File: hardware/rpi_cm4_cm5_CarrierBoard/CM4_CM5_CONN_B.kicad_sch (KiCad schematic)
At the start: 26 parts, among them J12 RPI_CMx_B

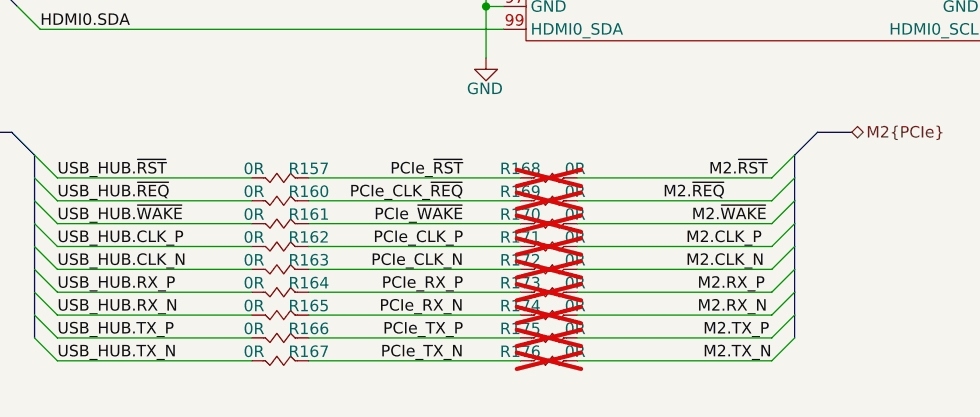
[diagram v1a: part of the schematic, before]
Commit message: Add preliminary output files (PCB PDF, Gerbers, IPC-D-356, IPC-2581, Pick_N_Place, etc) Update BOM, SCH PDF Commit PCB design and set to "Review" state
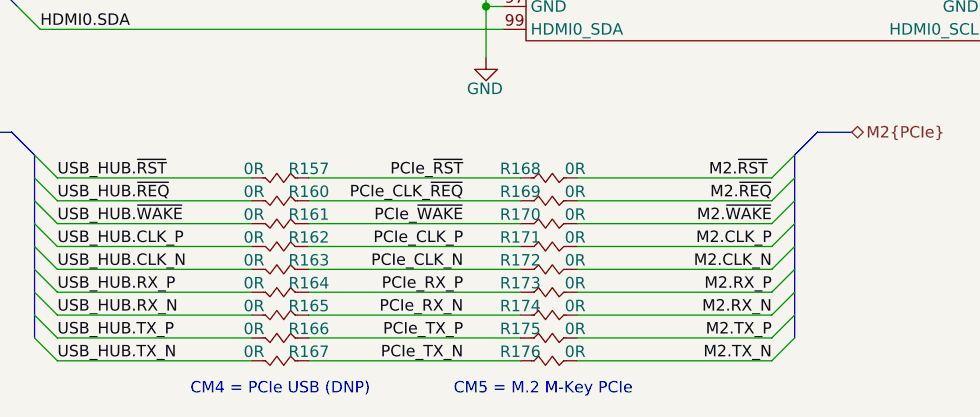
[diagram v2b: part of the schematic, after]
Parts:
- R168, R169, R170, R171, R172, R173, R174, R175, R176: now fitted
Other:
- note added: "CM4 = PCIe USB (DNP)"
- note added: "CM5 = M.2 M-Key PCIe"
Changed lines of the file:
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@@
 	(title_block
 		(title "RPI CMx Carrier")
-		(date "2026-02-13")
+		(date "2026-02-15")
 		(rev "2.00-0A")
 		(comment 1 "Jean-Francois Bilodeau")
@@
 		(comment 6 "Jean-Francois Bilodeau")
 		(comment 7 "Not applicable")
-		(comment 8 "Preliminary")
+		(comment 8 "Released")
 		(comment 9 "RPI_CMx_Carrier_2.00-0A_BOM")
 	)
@@
 		)
 	)
+	(text "CM4 = PCIe USB (DNP)"
+		(exclude_from_sim no)
+		(at 100.33 189.23 0)
+		(effects
+			(font
+				(size 1.27 1.27)
+				(color 255 153 0 1)
+			)
+		)
+	)
+	(text "CM5 = M.2 M-Key PCIe"
+		(exclude_from_sim no)
+		(at 129.54 189.23 0)
+		(effects
+			(font
+				(size 1.27 1.27)
+				(color 255 153 0 1)
+			)
+		)
+	)
 	(junction
 		(at 182.88 55.245)
@@
 	)
 	(label "M2.~{WAKE}"
-		(at 146.05 170.815 0)
+		(at 154.94 170.815 180)
 		(effects
 			(font
 				(size 1.27 1.27)
 			)
-			(justify left bottom)
+			(justify right bottom)
 		)
 	)
@@
 	)
 	(label "M2.CLK_N"
-		(at 145.415 175.895 0)
+		(at 154.94 175.895 180)
 		(effects
 			(font
 				(size 1.27 1.27)
 			)
-			(justify left bottom)
+			(justify right bottom)
 		)
 	)
@@
 	)
 	(label "M2.CLK_P"
-		(at 145.415 173.355 0)
+		(at 154.94 173.355 180)
 		(effects
 			(font
 				(size 1.27 1.27)
 			)
-			(justify left bottom)
+			(justify right bottom)
 		)
 	)
@@
 	)
 	(label "M2.TX_N"
-		(at 147.32 186.055 0)
+		(at 154.94 186.055 180)
 		(effects
 			(font
 				(size 1.27 1.27)
 			)
-			(justify left bottom)
+			(justify right bottom)
 		)
 	)
@@
 	)
 	(label "M2.~{REQ}"
-		(at 142.875 168.275 0)
+		(at 154.94 168.275 180)
 		(effects
 			(font
 				(size 1.27 1.27)
 			)
-			(justify left bottom)
+			(justify right bottom)
 		)
 	)
@@
 	)
 	(label "M2.TX_P"
-		(at 147.32 183.515 0)
+		(at 154.94 183.515 180)
 		(effects
 			(font
 				(size 1.27 1.27)
 			)
-			(justify left bottom)
+			(justify right bottom)
 		)
 	)
 	(label "M2.RX_P"
-		(at 146.685 178.435 0)
+		(at 154.94 178.435 180)
 		(effects
 			(font
 				(size 1.27 1.27)
 			)
-			(justify left bottom)
+			(justify right bottom)
 		)
 	)
 	(label "M2.RX_N"
-		(at 146.685 180.975 0)
+		(at 154.94 180.975 180)
 		(effects
 			(font
 				(size 1.27 1.27)
 			)
-			(justify left bottom)
+			(justify right bottom)
 		)
 	)
@@
 		(in_bom yes)
 		(on_board yes)
-		(dnp yes)
+		(dnp no)
 		(property "Reference" "R176"
 			(at 127 185.039 0)
@@
 		(in_bom yes)
 		(on_board yes)
-		(dnp yes)
+		(dnp no)
 		(property "Reference" "R173"
 			(at 127 177.419 0)
@@
 		(in_bom yes)
 		(on_board yes)
-		(dnp yes)
+		(dnp no)
 		(property "Reference" "R168"
 			(at 127 164.719 0)
@@
 		(in_bom yes)
 		(on_board yes)
-		(dnp yes)
+		(dnp no)
 		(property "Reference" "R171"
 			(at 127 172.339 0)
@@
 		(in_bom yes)
 		(on_board yes)
-		(dnp yes)
+		(dnp no)
 		(property "Reference" "R174"
 			(at 127 179.959 0)
@@
 		(in_bom yes)
 		(on_board yes)
-		(dnp yes)
+		(dnp no)
 		(property "Reference" "R172"
 			(at 127 174.879 0)
@@
 		(in_bom yes)
 		(on_board yes)
-		(dnp yes)
+		(dnp no)
 		(property "Reference" "R169"
 			(at 127 167.259 0)
@@
 		(in_bom yes)
 		(on_board yes)
-		(dnp yes)
+		(dnp no)
 		(property "Reference" "R175"
 			(at 127 182.499 0)
@@
 		(in_bom yes)
 		(on_board yes)
-		(dnp yes)
+		(dnp no)
 		(property "Reference" "R170"
 			(at 127 169.799 0)

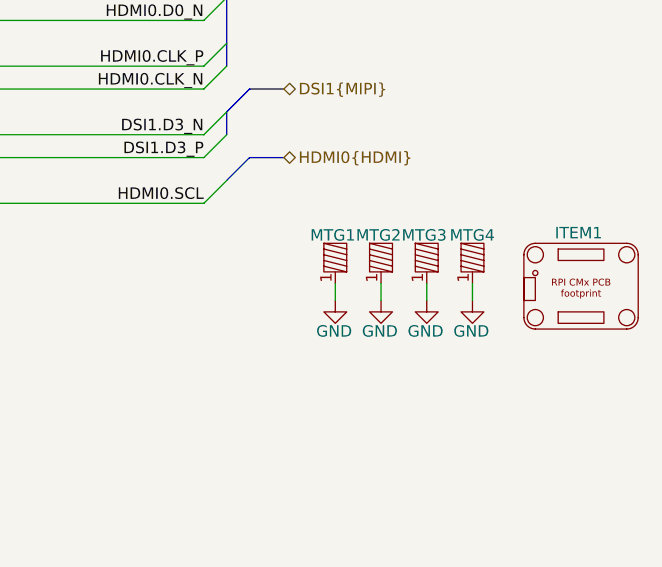
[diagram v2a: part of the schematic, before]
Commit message: Add test points on relevant signals Re-generate SCH_PDF Re-generate BOM Re-generate all gerbers and relevant PCB output files (still in review phase)
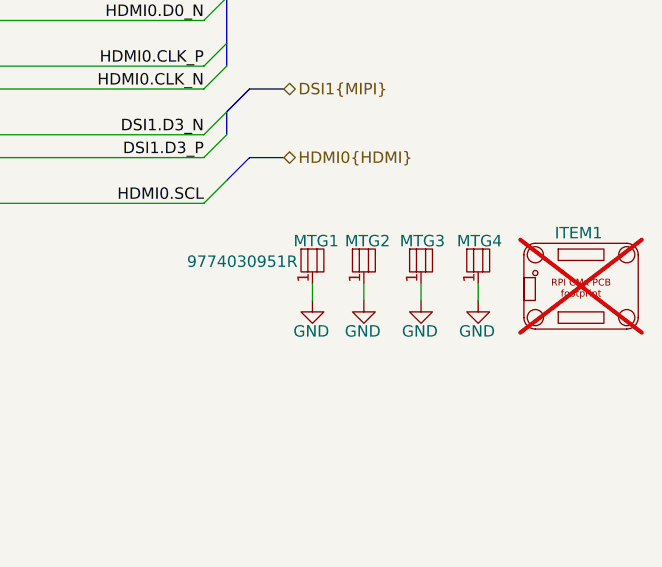
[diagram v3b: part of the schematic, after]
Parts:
- removed MTG1, MTG2, MTG3, MTG4: 9774030151R, footprint:9774030151R, symbol KicadCompDb:Miscellaneous/MISC_00002
- added MTG1, MTG2, MTG3, MTG4: 9774030951R, footprint:9774030151R, symbol KicadCompDb:Miscellaneous/MISC_00010
- ITEM1: now not fitted
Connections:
- net GND: now also MTG1.1, MTG2.1, MTG3.1, MTG4.1
